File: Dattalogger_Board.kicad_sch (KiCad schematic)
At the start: 25 parts, among them U1 24LC1025, U2 DS1337S_, U3 24LC1025, U4 ATMEGA328P-AU, Y1 32.768 KHz, Y2 16 MHz

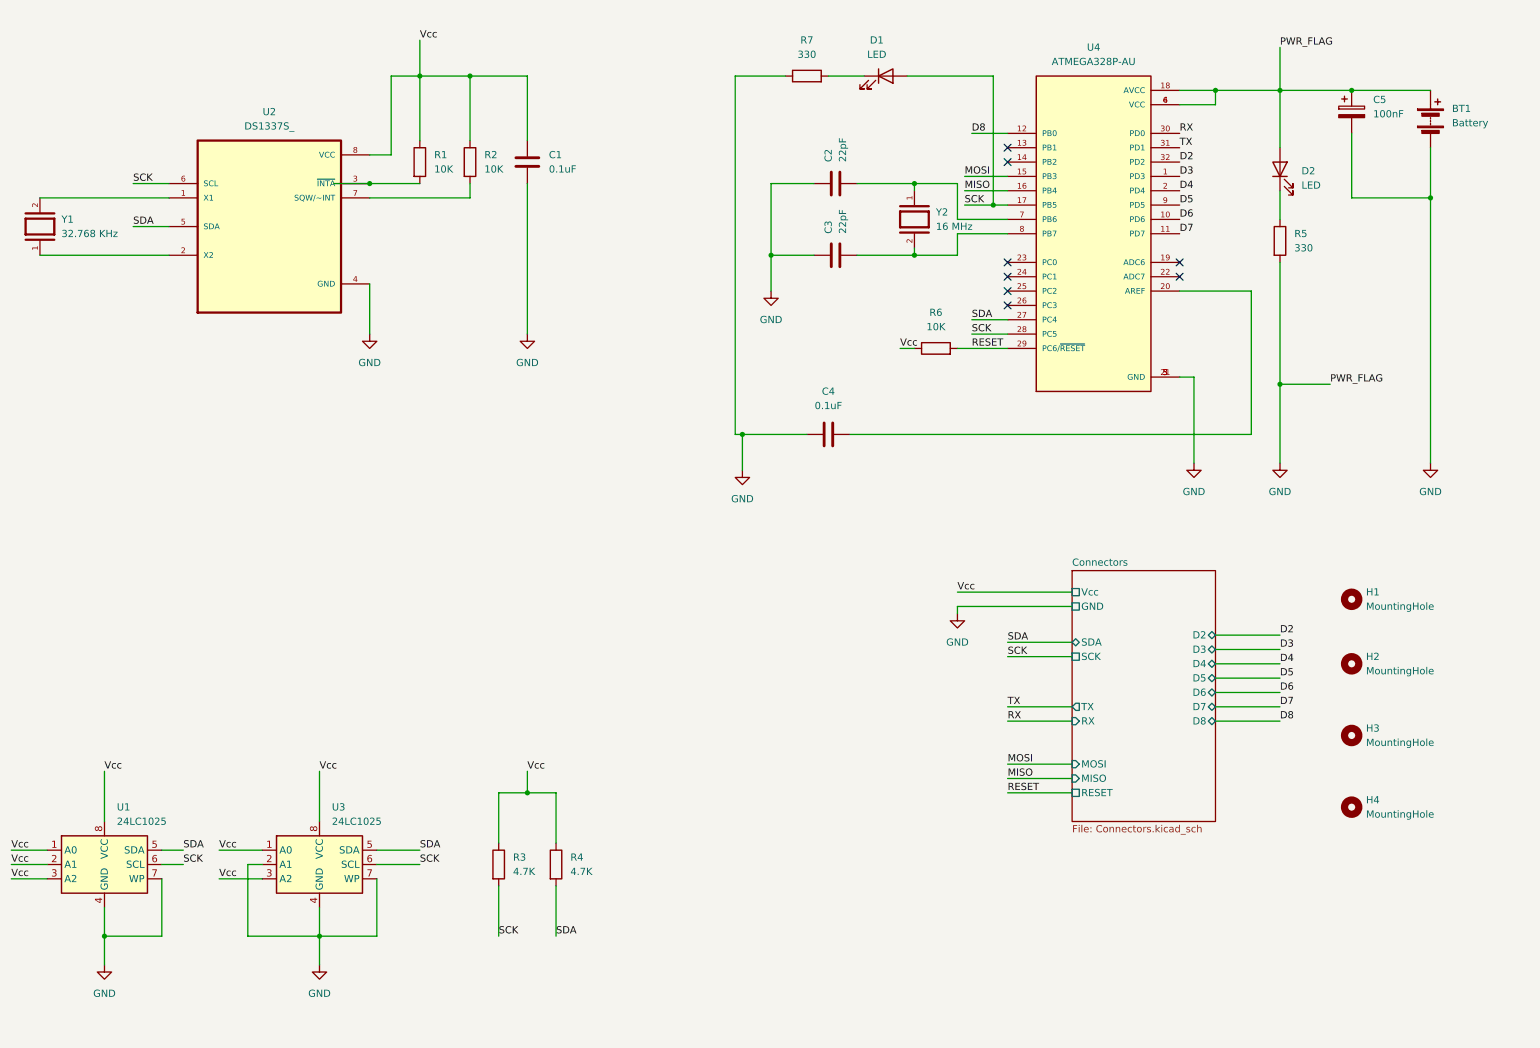
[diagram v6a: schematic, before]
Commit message: Addoed Power Flag and finished ERC
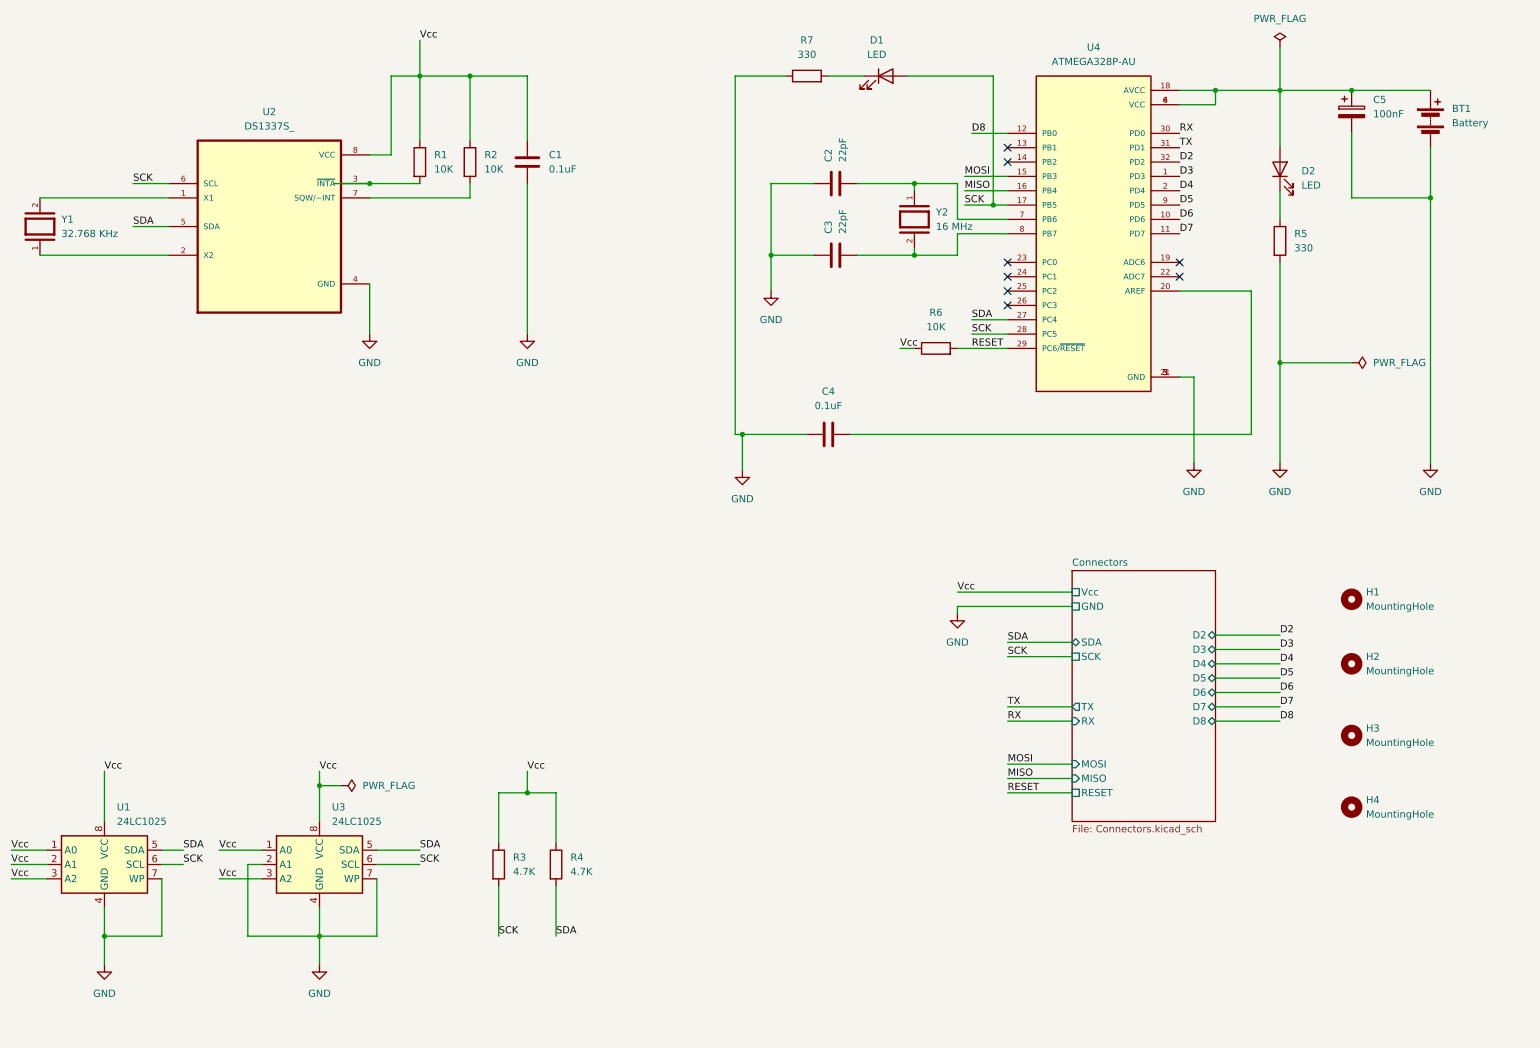
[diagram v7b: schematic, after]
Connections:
- net GND: no longer BT1.1 (+), C5.1, D2.2 (A), U4.18 (AVCC), U4.4 (VCC), U4.6 (VCC)
- new net: BT1.1 (+), C5.1, D2.2 (A), U4.18 (AVCC), U4.4 (VCC), U4.6 (VCC)
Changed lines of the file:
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@@
   (junction (at 80.01 44.45) (diameter 0) (color 0 0 0 0)
   )
+  (junction (at 241.3 76.2) (diameter 0) (color 0 0 0 0)
+  )
   (junction (at 176.53 44.45) (diameter 0) (color 0 0 0 0)
   )
@@
   (junction (at 33.02 177.8) (diameter 0) (color 0 0 0 0)
   )
-  (junction (at 241.3 80.01) (diameter 0) (color 0 0 0 0)
+  (junction (at 71.12 151.13) (diameter 0) (color 0 0 0 0)
   )
   (junction (at 146.05 88.9) (diameter 0) (color 0 0 0 0)
@@
     (stroke (width 0) (type default))
   )
+  (wire (pts (xy 241.3 76.2) (xy 241.3 93.98))
+    (stroke (width 0) (type default))
+  )
   (wire (pts (xy 184.15 44.45) (xy 176.53 44.45))
     (stroke (width 0) (type default))
@@
     (stroke (width 0) (type default))
   )
+  (wire (pts (xy 71.12 172.72) (xy 71.12 177.8))
+    (stroke (width 0) (type default))
+  )
   (wire (pts (xy 176.53 57.15) (xy 176.53 55.88))
     (stroke (width 0) (type default))
@@
     (stroke (width 0) (type default))
   )
-  (wire (pts (xy 241.3 58.42) (xy 241.3 80.01))
+  (wire (pts (xy 241.3 58.42) (xy 241.3 76.2))
     (stroke (width 0) (type default))
   )
@@
     (stroke (width 0) (type default))
   )
+  (wire (pts (xy 71.12 148.59) (xy 71.12 151.13))
+    (stroke (width 0) (type default))
+  )
   (wire (pts (xy 241.3 20.32) (xy 241.3 27.94))
     (stroke (width 0) (type default))
@@
     (stroke (width 0) (type default))
   )
-  (wire (pts (xy 241.3 80.01) (xy 241.3 93.98))
-    (stroke (width 0) (type default))
-  )
   (wire (pts (xy 151.13 57.15) (xy 158.75 57.15))
     (stroke (width 0) (type default))
   )
+  (wire (pts (xy 74.93 151.13) (xy 71.12 151.13))
+    (stroke (width 0) (type default))
+  )
   (wire (pts (xy 97.79 46.99) (xy 80.01 46.99))
     (stroke (width 0) (type default))
@@
     (stroke (width 0) (type default))
   )
-  (wire (pts (xy 71.12 177.8) (xy 71.12 172.72))
+  (wire (pts (xy 71.12 151.13) (xy 71.12 157.48))
     (stroke (width 0) (type default))
   )
@@
     (stroke (width 0) (type default))
   )
-  (wire (pts (xy 241.3 80.01) (xy 250.19 80.01))
-    (stroke (width 0) (type default))
-  )
   (wire (pts (xy 60.96 165.1) (xy 58.42 165.1))
     (stroke (width 0) (type default))
@@
     (stroke (width 0) (type default))
   )
-  (wire (pts (xy 71.12 148.59) (xy 71.12 157.48))
-    (stroke (width 0) (type default))
-  )
   (wire (pts (xy 223.52 30.48) (xy 229.87 30.48))
     (stroke (width 0) (type default))
@@
     (stroke (width 0) (type default))
   )
+  (wire (pts (xy 241.3 76.2) (xy 254 76.2))
+    (stroke (width 0) (type default))
+  )
   (wire (pts (xy 166.37 57.15) (xy 176.53 57.15))
     (stroke (width 0) (type default))
@@
     (effects (font (size 1.27 1.27)) (justify left bottom))
   )
-  (label "PWR_FLAG" (at 241.3 20.32 0) (fields_autoplaced)
-    (effects (font (size 1.27 1.27)) (justify left bottom))
-  )
   (label "Vcc" (at 107.95 148.59 0) (fields_autoplaced)
     (effects (font (size 1.27 1.27)) (justify left bottom))
@@
   )
   (label "SCK" (at 185.42 48.26 0) (fields_autoplaced)
-    (effects (font (size 1.27 1.27)) (justify left bottom))
-  )
-  (label "PWR_FLAG" (at 250.19 80.01 0) (fields_autoplaced)
     (effects (font (size 1.27 1.27)) (justify left bottom))
   )
@@
         (path "/a55893b1-5494-496a-9815-de4061e18fde"
           (reference "H3") (unit 1)
+        )
+      )
+    )
+  )
+  (symbol (lib_id "power:PWR_FLAG") (at 254 76.2 270) (unit 1)
+    (in_bom yes) (on_board yes) (dnp no) (fields_autoplaced)
+    (property "Reference" "#FLG01" (at 255.905 76.2 0)
+      (effects (font (size 1.27 1.27)) hide)
+    )
+    (property "Value" "PWR_FLAG" (at 257.81 76.2 90)
+      (effects (font (size 1.27 1.27)) (justify left))
+    )
+    (property "Footprint" "" (at 254 76.2 0)
+      (effects (font (size 1.27 1.27)) hide)
+    )
+    (property "Datasheet" "~" (at 254 76.2 0)
+      (effects (font (size 1.27 1.27)) hide)
+    )
+    (pin "1")
+    (instances
+      (project "Dattalogger_Board"
+        (path "/a55893b1-5494-496a-9815-de4061e18fde"
+          (reference "#FLG01") (unit 1)
         )
       )
@@
         (path "/a55893b1-5494-496a-9815-de4061e18fde"
           (reference "R3") (unit 1)
+        )
+      )
+    )
+  )
+  (symbol (lib_id "power:PWR_FLAG") (at 74.93 151.13 270) (unit 1)
+    (in_bom yes) (on_board yes) (dnp no) (fields_autoplaced)
+    (property "Reference" "#FLG03" (at 76.835 151.13 0)
+      (effects (font (size 1.27 1.27)) hide)
+    )
+    (property "Value" "PWR_FLAG" (at 78.74 151.13 90)
+      (effects (font (size 1.27 1.27)) (justify left))
+    )
+    (property "Footprint" "" (at 74.93 151.13 0)
+      (effects (font (size 1.27 1.27)) hide)
+    )
+    (property "Datasheet" "~" (at 74.93 151.13 0)
+      (effects (font (size 1.27 1.27)) hide)
+    )
+    (pin "1")
+    (instances
+      (project "Dattalogger_Board"
+        (path "/a55893b1-5494-496a-9815-de4061e18fde"
+          (reference "#FLG03") (unit 1)
         )
       )
@@
         )
       )
+    )
+  )
+  (symbol (lib_id "power:PWR_FLAG") (at 241.3 20.32 0) (unit 1)
+    (in_bom yes) (on_board yes) (dnp no) (fields_autoplaced)
+    (property "Reference" "#FLG02" (at 241.3 18.415 0)
+      (effects (font (size 1.27 1.27)) hide)
+    )
+    (property "Value" "PWR_FLAG" (at 241.3 15.24 0)
+      (effects (font (size 1.27 1.27)))
+    )
+    (property "Footprint" "" (at 241.3 20.32 0)
+      (effects (font (size 1.27 1.27)) hide)
+    )
+    (property "Datasheet" "~" (at 241.3 20.32 0)
+      (effects (font (size 1.27 1.27)) hide)
+    )
+    (pin "1")
+    (instances
+      (project "Dattalogger_Board"
+        (path "/a55893b1-5494-496a-9815-de4061e18fde"
+          (reference "#FLG02") (unit 1)
+        )
+      )

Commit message: Completed comments
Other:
- note added: "EEPROM ( Memory )"
- note added: "MCU"
- note added: "Mounting ( Mechanical )"
- note added: "Real Time Clock"
- moved on the sheet: D1, H1, H2, H3, H4, R3, R4, R7, U1, U3
